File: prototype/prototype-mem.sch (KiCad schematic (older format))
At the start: 1 part

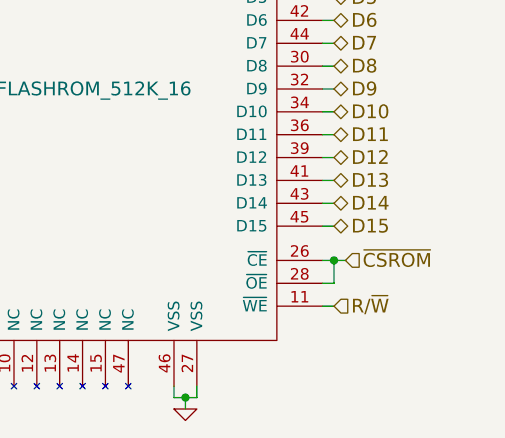
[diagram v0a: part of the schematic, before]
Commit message: Use separate read-enable and write-enable symbols for memory.
Previously we tried to infer these from a combination of the chip select
and R/W signals, but that's not possible without additional glue logic so
we'll just put two more pins on the FPGA output and do the glue logic in
there instead.
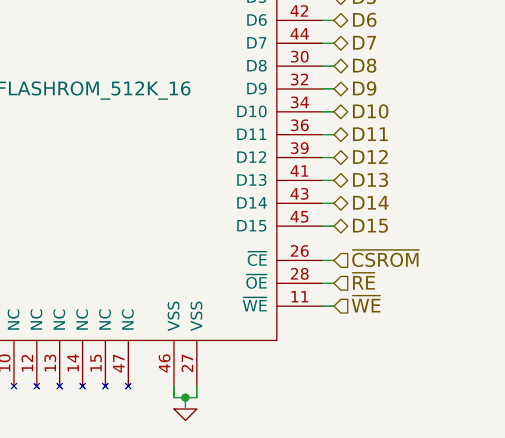
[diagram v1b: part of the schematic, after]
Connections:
- net ~CSROM: no longer U?.28 (~OE)
- net R/~W renamed ~WE
- new net ~RE: U?.28 (~OE)
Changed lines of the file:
@@
 $EndComp
-Wire Wire Line
-	5750 3650 5650 3650
-Wire Wire Line
-	5700 3650 5700 3750
-Wire Wire Line
-	5700 3750 5650 3750
-Connection ~ 5700 3650
 Wire Wire Line
 	5650 3850 5700 3850
@@
 Text HLabel 5700 3500 2    60   BiDi ~ 0
 D15
-Text HLabel 5750 3650 2    60   Input ~ 0
+Text HLabel 5700 3650 2    60   Input ~ 0
 ~CSROM
 Text HLabel 5700 3850 2    60   Input ~ 0
-R/~W
+~WE
+Text HLabel 5700 3750 2    60   Input ~ 0
+~RE
+Wire Wire Line
+	5650 3650 5700 3650
+Wire Wire Line
+	5650 3750 5700 3750
 $EndSCHEMATC

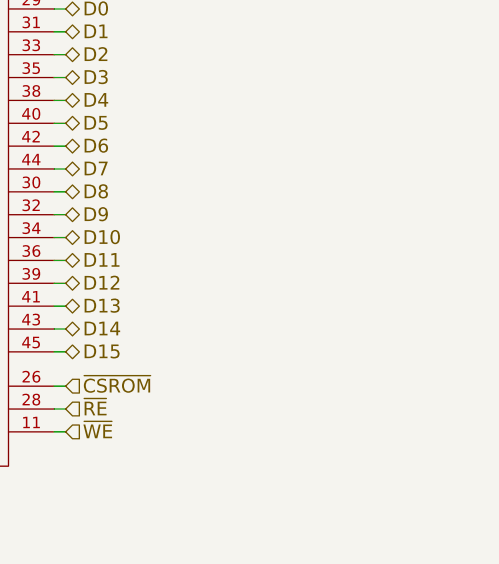
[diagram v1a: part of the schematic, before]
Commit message: Add placeholders for the RAM chip-selects.
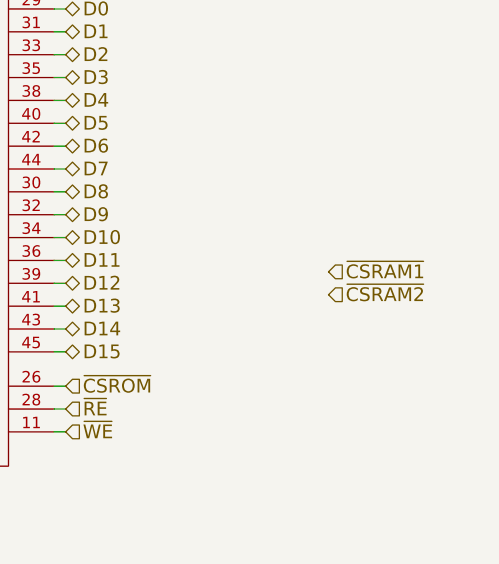
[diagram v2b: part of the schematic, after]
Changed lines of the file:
@@
 Wire Wire Line
 	5650 3750 5700 3750
+Text HLabel 6850 3150 2    60   Input ~ 0
+~CSRAM1
+Text HLabel 6850 3250 2    60   Input ~ 0
+~CSRAM2
 $EndSCHEMATC

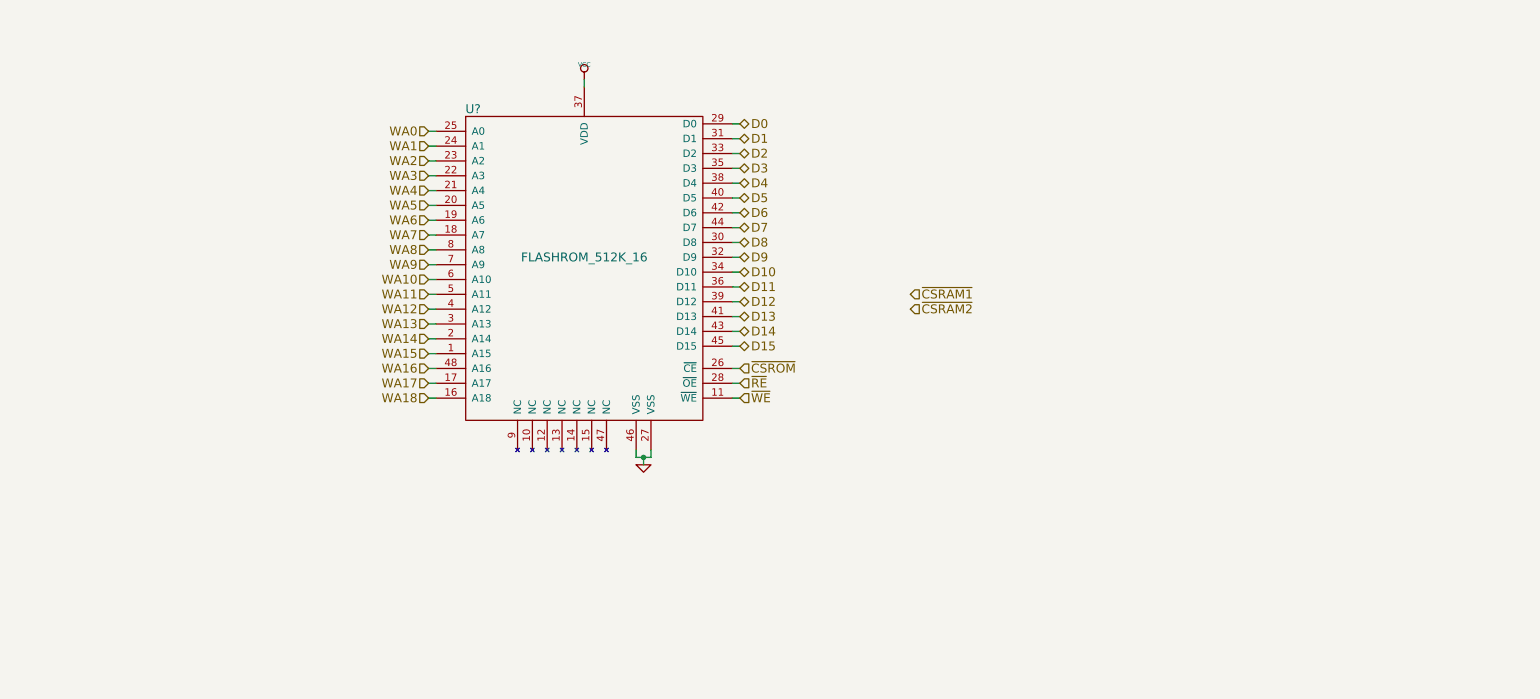
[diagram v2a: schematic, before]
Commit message: RAM chip schematic.
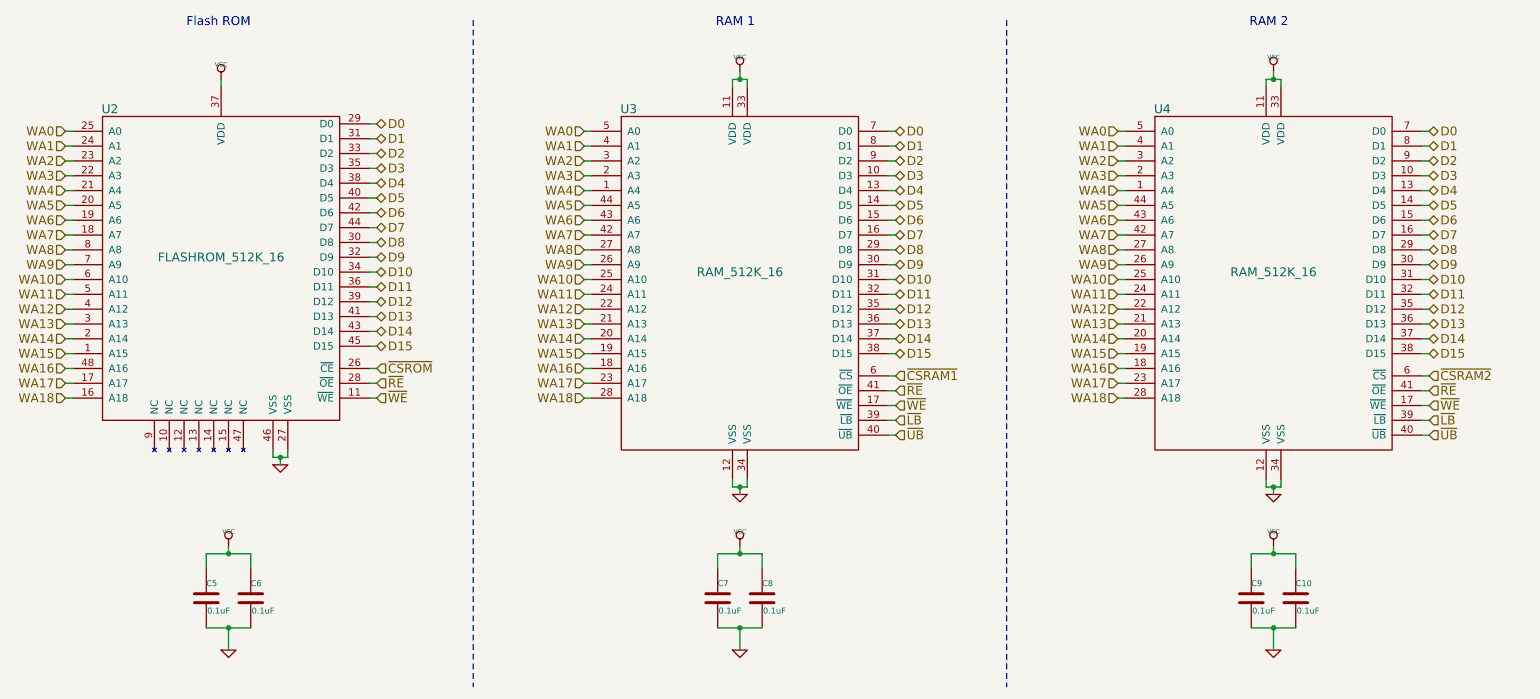
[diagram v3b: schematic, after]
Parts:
- added C10, C5, C6, C7, C8, C9: 0.1uF, symbol C
- added U3, U4: RAM_512K_16, symbol RAM_512K_16
- gave numbers to parts that had none: 1
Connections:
- net D0: now also U3.7 (D0), U4.7 (D0)
- net D1: now also U3.8 (D1), U4.8 (D1)
- net D10: now also U3.31 (D10), U4.31 (D10)
- net D11: now also U3.32 (D11), U4.32 (D11)
- net D12: now also U3.35 (D12), U4.35 (D12)
- net D13: now also U3.36 (D13), U4.36 (D13)
- net D14: now also U3.37 (D14), U4.37 (D14)
- net D15: now also U3.38 (D15), U4.38 (D15)
- net D2: now also U3.9 (D2), U4.9 (D2)
- net D3: now also U3.10 (D3), U4.10 (D3)
- net D4: now also U3.13 (D4), U4.13 (D4)
- net D5: now also U3.14 (D5), U4.14 (D5)
- net D6: now also U3.15 (D6), U4.15 (D6)
- net D7: now also U3.16 (D7), U4.16 (D7)
- net D8: now also U3.29 (D8), U4.29 (D8)
- net D9: now also U3.30 (D9), U4.30 (D9)
- net GND: now also C10.2, C5.2, C6.2, C7.2, C8.2, C9.2, U3.12 (VSS), U3.34 (VSS), U4.12 (VSS), U4.34 (VSS)
- net VCC: now also C10.1, C5.1, C6.1, C7.1, C8.1, C9.1, U3.11 (VDD), U3.33 (VDD), U4.11 (VDD), U4.33 (VDD)
- net WA0: now also U3.5 (A0), U4.5 (A0)
- net WA1: now also U3.4 (A1), U4.4 (A1)
- net WA10: now also U3.25 (A10), U4.25 (A10)
- net WA11: now also U3.24 (A11), U4.24 (A11)
- net WA12: now also U3.22 (A12), U4.22 (A12)
- net WA13: now also U3.21 (A13), U4.21 (A13)
- net WA14: now also U3.20 (A14), U4.20 (A14)
- net WA15: now also U3.19 (A15), U4.19 (A15)
- net WA16: now also U3.18 (A16), U4.18 (A16)
- net WA17: now also U3.23 (A17), U4.23 (A17)
- net WA18: now also U3.28 (A18), U4.28 (A18)
- net WA2: now also U3.3 (A2), U4.3 (A2)
- net WA3: now also U3.2 (A3), U4.2 (A3)
- net WA4: now also U3.1 (A4), U4.1 (A4)
- net WA5: now also U3.44 (A5), U4.44 (A5)
- net WA6: now also U3.43 (A6), U4.43 (A6)
- net WA7: now also U3.42 (A7), U4.42 (A7)
- net WA8: now also U3.27 (A8), U4.27 (A8)
- net WA9: now also U3.26 (A9), U4.26 (A9)
- net ~CSRAM1: now also U3.6 (~CS)
- net ~CSRAM2: now also U4.6 (~CS)
- net ~RE: now also U3.41 (~OE), U4.41 (~OE)
- net ~WE: now also U3.17 (~WE), U4.17 (~WE)
- new net ~LB: U3.39 (~LB), U4.39 (~LB)
- new net ~UB: U3.40 (~UB), U4.40 (~UB)
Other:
- note added: "Flash ROM"
- note added: "RAM 1"
- note added: "RAM 2"
- moved on the sheet: U2

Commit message: Move some bits around for easier PCB layout.
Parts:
- C10, C5, C6, C7, C8, C9: footprint (none) -> Capacitors_SMD:C_0805_HandSoldering
- U2: footprint (none) -> SSOP_Packages:TSSOP-48_6.1x12.5mm_Pitch0.5mm
- U3, U4: footprint (none) -> SMD_Packages:PLCC-44
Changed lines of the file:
@@
 F 0 "U2" H 1450 3900 60  0000 C CNN
 F 1 "FLASHROM_512K_16" H 2200 2900 60  0000 C CNN
-F 2 "" H 1650 2900 60  0000 C CNN
+F 2 "SSOP_Packages:TSSOP-48_6.1x12.5mm_Pitch0.5mm" H 1650 2900 60  0001 C CNN
 F 3 "" H 1650 2900 60  0000 C CNN
 	1    2200 2900
@@
 	3200 3850 3250 3850
 $Comp
-L GND #PWR24
+L GND #PWR021
 U 1 1 551A445A
 P 2600 4300
-F 0 "#PWR24" H 2600 4300 30  0001 C CNN
+F 0 "#PWR021" H 2600 4300 30  0001 C CNN
 F 1 "GND" H 2600 4230 30  0001 C CNN
 F 2 "" H 2600 4300 60  0000 C CNN
@@
 Connection ~ 2600 4250
 $Comp
-L VCC #PWR21
+L VCC #PWR022
 U 1 1 551A4465
 P 2200 1700
-F 0 "#PWR21" H 2200 1800 30  0001 C CNN
+F 0 "#PWR022" H 2200 1800 30  0001 C CNN
 F 1 "VCC" H 2200 1800 30  0000 C CNN
 F 2 "" H 2200 1700 60  0000 C CNN
@@
 F 0 "C5" H 2100 5300 40  0000 L CNN
 F 1 "0.1uF" H 2106 5115 40  0000 L CNN
-F 2 "" H 2138 5050 30  0000 C CNN
+F 2 "Capacitors_SMD:C_0805_HandSoldering" H 2138 5050 30  0001 C CNN
 F 3 "" H 2100 5200 60  0000 C CNN
 	1    2100 5200
@@
 F 0 "C6" H 2400 5300 40  0000 L CNN
 F 1 "0.1uF" H 2406 5115 40  0000 L CNN
-F 2 "" H 2438 5050 30  0000 C CNN
+F 2 "Capacitors_SMD:C_0805_HandSoldering" H 2438 5050 30  0001 C CNN
 F 3 "" H 2400 5200 60  0000 C CNN
 	1    2400 5200
@@
 $EndComp
 $Comp
-L VCC #PWR22
+L VCC #PWR023
 U 1 1 551B8DC6
 P 2250 4850
-F 0 "#PWR22" H 2250 4950 30  0001 C CNN
+F 0 "#PWR023" H 2250 4950 30  0001 C CNN
 F 1 "VCC" H 2250 4950 30  0000 C CNN
 F 2 "" H 2250 4850 60  0000 C CNN
@@
 $EndComp
 $Comp
-L GND #PWR23
+L GND #PWR024
 U 1 1 551B8DED
 P 2250 5550
-F 0 "#PWR23" H 2250 5550 30  0001 C CNN
+F 0 "#PWR024" H 2250 5550 30  0001 C CNN
 F 1 "GND" H 2250 5480 30  0001 C CNN
 F 2 "" H 2250 5550 60  0000 C CNN
@@
 F 0 "U3" H 4950 4100 60  0000 C CNN
 F 1 "RAM_512K_16" H 5700 3000 60  0000 C CNN
-F 2 "" H 5150 3100 60  0000 C CNN
+F 2 "SMD_Packages:PLCC-44" H 5150 3100 60  0001 C CNN
 F 3 "" H 5150 3100 60  0000 C CNN
 	1    5700 3000
@@
 F 0 "U4" H 8550 4100 60  0000 C CNN
 F 1 "RAM_512K_16" H 9300 3000 60  0000 C CNN
-F 2 "" H 8750 3100 60  0000 C CNN
+F 2 "SMD_Packages:PLCC-44" H 8750 3100 60  0001 C CNN
 F 3 "" H 8750 3100 60  0000 C CNN
 	1    9300 3000
@@
 	10300 4100 10350 4100
 $Comp
-L VCC #PWR29
+L VCC #PWR025
 U 1 1 551BB608
 P 9300 1650
-F 0 "#PWR29" H 9300 1750 30  0001 C CNN
+F 0 "#PWR025" H 9300 1750 30  0001 C CNN
 F 1 "VCC" H 9300 1750 30  0000 C CNN
 F 2 "" H 9300 1650 60  0000 C CNN
@@
 $EndComp
 $Comp
-L VCC #PWR25
+L VCC #PWR026
 U 1 1 551BB624
 P 5700 1650
-F 0 "#PWR25" H 5700 1750 30  0001 C CNN
+F 0 "#PWR026" H 5700 1750 30  0001 C CNN
 F 1 "VCC" H 5700 1750 30  0000 C CNN
 F 2 "" H 5700 1650 60  0000 C CNN
@@
 Connection ~ 5700 1700
 $Comp
-L GND #PWR26
+L GND #PWR027
 U 1 1 551BB92A
 P 5700 4500
-F 0 "#PWR26" H 5700 4500 30  0001 C CNN
+F 0 "#PWR027" H 5700 4500 30  0001 C CNN
 F 1 "GND" H 5700 4430 30  0001 C CNN
 F 2 "" H 5700 4500 60  0000 C CNN
@@
 $EndComp
 $Comp
-L GND #PWR30
+L GND #PWR028
 U 1 1 551BB96B
 P 9300 4500
-F 0 "#PWR30" H 9300 4500 30  0001 C CNN
+F 0 "#PWR028" H 9300 4500 30  0001 C CNN
 F 1 "GND" H 9300 4430 30  0001 C CNN
 F 2 "" H 9300 4500 60  0000 C CNN
@@
 F 0 "C7" H 5550 5300 40  0000 L CNN
 F 1 "0.1uF" H 5556 5115 40  0000 L CNN
-F 2 "" H 5588 5050 30  0000 C CNN
+F 2 "Capacitors_SMD:C_0805_HandSoldering" H 5588 5050 30  0001 C CNN
 F 3 "" H 5550 5200 60  0000 C CNN
 	1    5550 5200
@@
 F 0 "C8" H 5850 5300 40  0000 L CNN
 F 1 "0.1uF" H 5856 5115 40  0000 L CNN
-F 2 "" H 5888 5050 30  0000 C CNN
+F 2 "Capacitors_SMD:C_0805_HandSoldering" H 5888 5050 30  0001 C CNN
 F 3 "" H 5850 5200 60  0000 C CNN
 	1    5850 5200
@@
 $EndComp
 $Comp
-L VCC #PWR27
+L VCC #PWR029
 U 1 1 551BBECA
 P 5700 4850
-F 0 "#PWR27" H 5700 4950 30  0001 C CNN
+F 0 "#PWR029" H 5700 4950 30  0001 C CNN
 F 1 "VCC" H 5700 4950 30  0000 C CNN
 F 2 "" H 5700 4850 60  0000 C CNN
@@
 $EndComp
 $Comp
-L GND #PWR28
+L GND #PWR030
 U 1 1 551BBED0
 P 5700 5550
-F 0 "#PWR28" H 5700 5550 30  0001 C CNN
+F 0 "#PWR030" H 5700 5550 30  0001 C CNN
 F 1 "GND" H 5700 5480 30  0001 C CNN
 F 2 "" H 5700 5550 60  0000 C CNN
@@
 F 0 "C9" H 9150 5300 40  0000 L CNN
 F 1 "0.1uF" H 9156 5115 40  0000 L CNN
-F 2 "" H 9188 5050 30  0000 C CNN
+F 2 "Capacitors_SMD:C_0805_HandSoldering" H 9188 5050 30  0001 C CNN
 F 3 "" H 9150 5200 60  0000 C CNN
 	1    9150 5200
@@
 F 0 "C10" H 9450 5300 40  0000 L CNN
 F 1 "0.1uF" H 9456 5115 40  0000 L CNN
-F 2 "" H 9488 5050 30  0000 C CNN
+F 2 "Capacitors_SMD:C_0805_HandSoldering" H 9488 5050 30  0001 C CNN
 F 3 "" H 9450 5200 60  0000 C CNN
 	1    9450 5200
@@
 $EndComp
 $Comp
-L VCC #PWR31
+L VCC #PWR031
 U 1 1 551BC238
 P 9300 4850
-F 0 "#PWR31" H 9300 4950 30  0001 C CNN
+F 0 "#PWR031" H 9300 4950 30  0001 C CNN
 F 1 "VCC" H 9300 4950 30  0000 C CNN
 F 2 "" H 9300 4850 60  0000 C CNN
@@
 $EndComp
 $Comp
-L GND #PWR32
+L GND #PWR032
 U 1 1 551BC23E
 P 9300 5550
-F 0 "#PWR32" H 9300 5550 30  0001 C CNN
+F 0 "#PWR032" H 9300 5550 30  0001 C CNN
 F 1 "GND" H 9300 5480 30  0001 C CNN
 F 2 "" H 9300 5550 60  0000 C CNN

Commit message: Assign appropriate footprints to the memory ICs.
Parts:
- U2: footprint SSOP_Packages:TSSOP-48_6.1x12.5mm_Pitch0.5mm -> 68k-computer:TSOP-48
- U3, U4: footprint SMD_Packages:PLCC-44 -> 68k-computer:TSOP-44
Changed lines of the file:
@@
 F 0 "U2" H 1450 3900 60  0000 C CNN
 F 1 "FLASHROM_512K_16" H 2200 2900 60  0000 C CNN
-F 2 "SSOP_Packages:TSSOP-48_6.1x12.5mm_Pitch0.5mm" H 1650 2900 60  0001 C CNN
+F 2 "68k-computer:TSOP-48" H 1650 2900 60  0001 C CNN
 F 3 "" H 1650 2900 60  0000 C CNN
 	1    2200 2900
@@
 F 0 "U3" H 4950 4100 60  0000 C CNN
 F 1 "RAM_512K_16" H 5700 3000 60  0000 C CNN
-F 2 "SMD_Packages:PLCC-44" H 5150 3100 60  0001 C CNN
+F 2 "68k-computer:TSOP-44" H 5150 3100 60  0001 C CNN
 F 3 "" H 5150 3100 60  0000 C CNN
 	1    5700 3000
@@
 F 0 "U4" H 8550 4100 60  0000 C CNN
 F 1 "RAM_512K_16" H 9300 3000 60  0000 C CNN
-F 2 "SMD_Packages:PLCC-44" H 8750 3100 60  0001 C CNN
+F 2 "68k-computer:TSOP-44" H 8750 3100 60  0001 C CNN
 F 3 "" H 8750 3100 60  0000 C CNN
 	1    9300 3000

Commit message: "Rescue" the schematic after a KiCad upgrade.
Some symbols changed in the new version.
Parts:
- C10, C5, C6, C7, C8, C9: symbol C -> C-RESCUE-prototype
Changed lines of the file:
@@
 EESchema Schematic File Version 2
+LIBS:prototype-rescue
 LIBS:power
 LIBS:device
@@
 LIBS:memory
 LIBS:xilinx
-LIBS:special
 LIBS:microcontrollers
 LIBS:dsp
@@
 	3200 3850 3250 3850
 $Comp
-L GND #PWR021
+L GND-RESCUE-prototype #PWR021
 U 1 1 551A445A
 P 2600 4300
@@
 ~CSRAM1
 $Comp
-L C C5
+L C-RESCUE-prototype C5
 U 1 1 551B8D70
 P 2100 5200
@@
 $EndComp
 $Comp
-L C C6
+L C-RESCUE-prototype C6
 U 1 1 551B8D9C
 P 2400 5200
@@
 $EndComp
 $Comp
-L GND #PWR024
+L GND-RESCUE-prototype #PWR024
 U 1 1 551B8DED
 P 2250 5550
@@
 Connection ~ 5700 1700
 $Comp
-L GND #PWR027
+L GND-RESCUE-prototype #PWR027
 U 1 1 551BB92A
 P 5700 4500
@@
 $EndComp
 $Comp
-L GND #PWR028
+L GND-RESCUE-prototype #PWR028
 U 1 1 551BB96B
 P 9300 4500
@@
 Connection ~ 5700 4450
 $Comp
-L C C7
+L C-RESCUE-prototype C7
 U 1 1 551BBEBE
 P 5550 5200
@@
 $EndComp
 $Comp
-L C C8
+L C-RESCUE-prototype C8
 U 1 1 551BBEC4
 P 5850 5200
@@
 $EndComp
 $Comp
-L GND #PWR030
+L GND-RESCUE-prototype #PWR030
 U 1 1 551BBED0
 P 5700 5550
@@
 Connection ~ 5700 5400
 $Comp
-L C C9
+L C-RESCUE-prototype C9
 U 1 1 551BC22C
 P 9150 5200
@@
 $EndComp
 $Comp
-L C C10
+L C-RESCUE-prototype C10
 U 1 1 551BC232
 P 9450 5200
@@
 $EndComp
 $Comp
-L GND #PWR032
+L GND-RESCUE-prototype #PWR032
 U 1 1 551BC23E
 P 9300 5550
